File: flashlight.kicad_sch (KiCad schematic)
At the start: 25 parts, among them J1 USB_B_Micro, J2 Conn_01x03_Pin, Q1 HSS2333, Q2 HSS2333, SW1 SW_DIP_x01, U1 LP4054HB5F, U2 MT3608

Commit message: tight sot23-6
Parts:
- removed R11: 10k, Resistor_SMD:R_0603_1608Metric, symbol Device:R
- U2: footprint Package_TO_SOT_SMD:SOT-23-6 -> SparkFun-Semiconductor-Standard:SOT23-6-Tight
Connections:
- net at C3.1, L1.1, SW1.2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: now also U2.4 (EN)
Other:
- moved on the sheet: C4, D5, L1, R6, R7, U2

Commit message: v2.4: double led
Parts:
- removed D2: CHARGING, LED_SMD:LED_0603_1608Metric, symbol Device:LED
- removed D3: CHARGED, LED_SMD:LED_0805_2012Metric, symbol Device:LED
- removed R3: 1k, Resistor_SMD:R_0805_2012Metric, symbol Device:R
- removed U1: LP4054HB5F, Package_TO_SOT_SMD:SOT-23-5, symbol Battery_Management:MCP73831-2-OT
- added U3: TP4057, Package_TO_SOT_SMD:SOT-23-6, symbol MySymbols:TP4057
- added U4: R6BHC-A05_LED-19-223, MyFootprints:R6BHC-A05_LED, symbol MySymbols_GLOB:R6BHC-A05_LED
- BT1: footprint FlashlightLib:BH-18650 -> FlashlightLib:BH-18650_NoHole; now not fitted
- J2, SW1: now not fitted
- L1: now in the parts list
- R1, R2: value 1k -> 2k2; footprint Resistor_SMD:R_0805_2012Metric -> Resistor_SMD:R_0603_1608Metric; LCSC C17513 -> C4190
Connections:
- net GND: now also U3.2 (GND)
- net at C2.1, Q1.3 (D), Q2.3 (D): now also U3.3 (BAT)
- net at R2.1: now also C1.1, D1.1 (K), D4.2 (A), Q2.1 (G), R4.1, U3.4 (VCC)
- net at R2.2: now also U4.1 (Blue+), U4.3 (Red+)
- net at R1.1: now also U3.6 (PROG)
- new net: U3.5 (STDBY), U4.2 (Blue-)
- new net: U3.1 (CHRG), U4.4 (Red-)

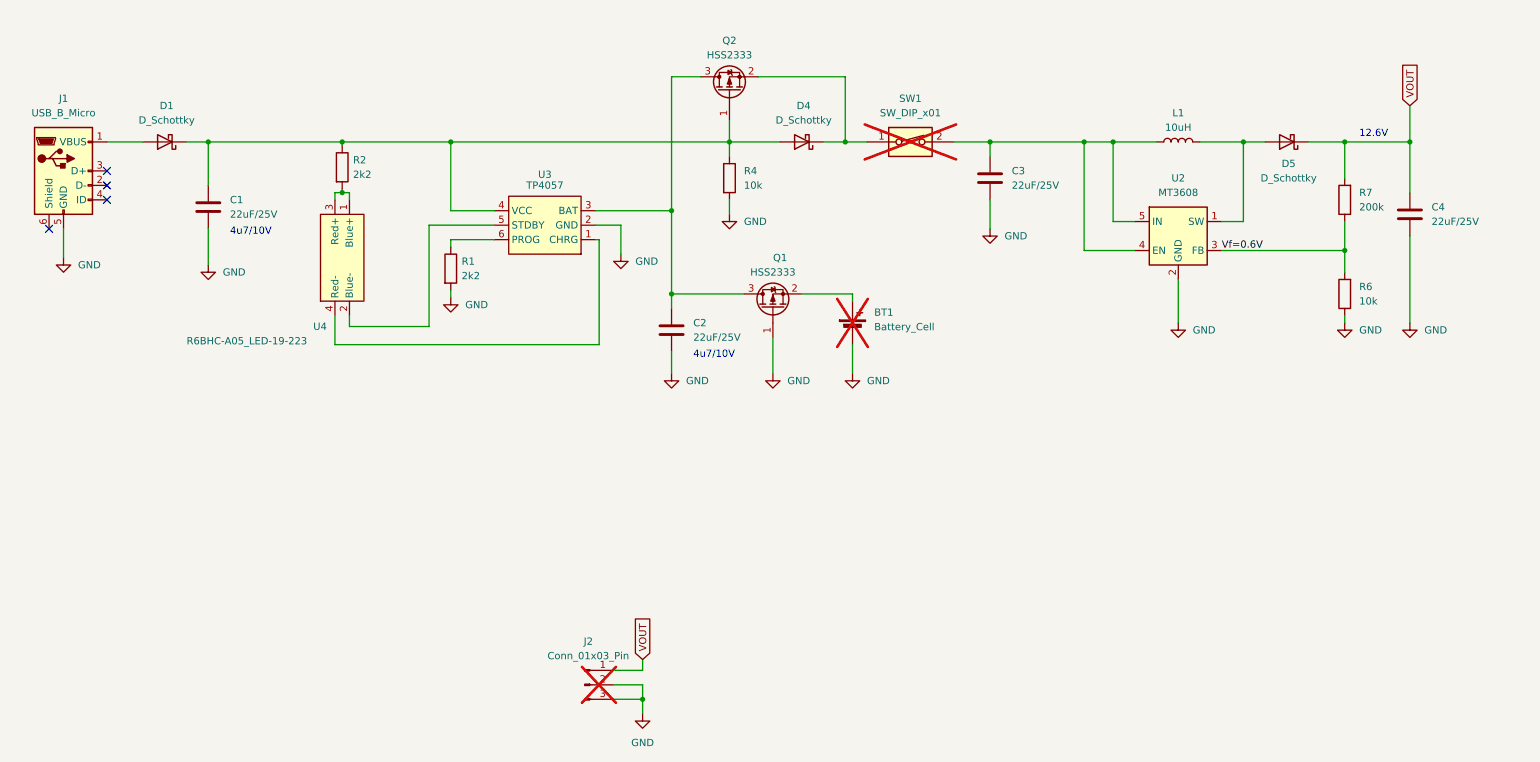
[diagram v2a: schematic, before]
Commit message: v2.4 xb4908A undervoltage protection
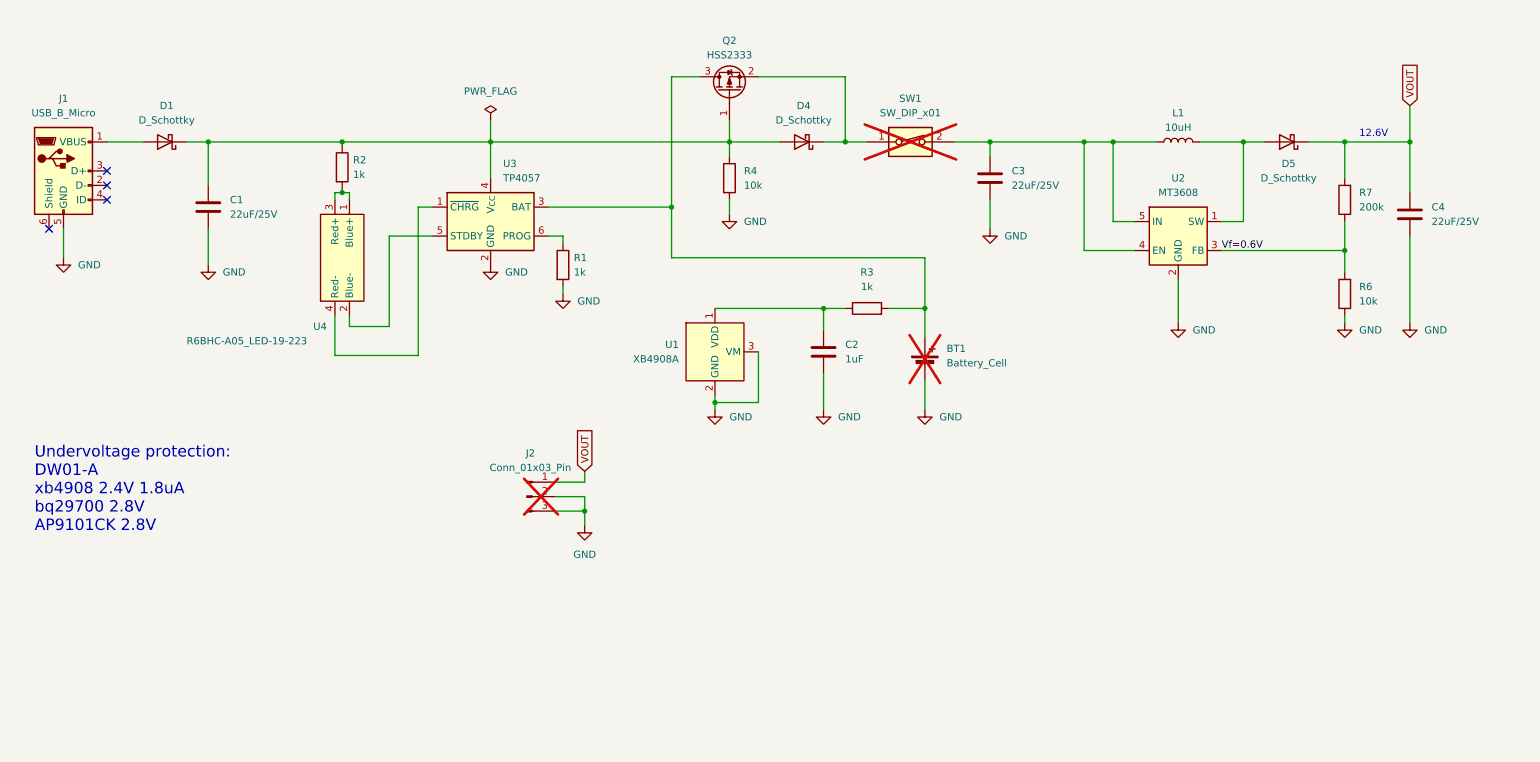
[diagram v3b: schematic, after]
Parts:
- removed Q1: HSS2333, Package_TO_SOT_SMD:SOT-23, symbol Transistor_FET:AO3401A
- removed U3: TP4057, Package_TO_SOT_SMD:SOT-23-6, symbol MySymbols:TP4057
- added R3: 1k, Resistor_SMD:R_0603_1608Metric, symbol Device:R
- added U1: XB4908A, FlashlightLib:XB4908A, symbol MySymbols:XB4908A
- added U3: TP4057, Package_TO_SOT_SMD:TSOT-23-6, symbol Battery_Management:TP4057
- C2: value 22uF/25V -> 1uF; footprint Capacitor_SMD:C_0805_2012Metric -> Capacitor_SMD:C_0603_1608Metric; LCSC C45783 -> C15849
- C3: LCSC C513764 -> C45783
- D5: LCSC C5338051 -> C22452
- R1, R2: value 2k2 -> 1k; LCSC C4190 -> C21190
- U2: footprint SparkFun-Semiconductor-Standard:SOT23-6-Tight -> Package_TO_SOT_SMD:SOT-23-6
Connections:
- net GND: now also U1.2 (GND), U1.3 (VM), U1.4 (VM), U3.2 (GND)
- net at C1.1, D1.1 (K), D4.2 (A)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: now also U3.4 (V_{CC})
- net at BT1.1 (+): now also Q2.3 (D), R3.2, U3.3 (BAT)
- net at C2.1: now also R3.1, U1.1 (VDD); no longer Q2.3 (D)
- net at U4.2 (Blue-): now also U3.5 (STDBY)
- net at U4.4 (Red-): now also U3.1 (~{CHRG})
- net at R1.1: now also U3.6 (PROG)
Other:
- note added: "Undervoltage protection: DW01-A xb4908 2.4V 1.8uA bq29700 2.8V AP9101CK 2.8V"
- note removed: "4u7/10V"
- moved on the sheet: BT1, C2, J2, R1

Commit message: increased 18650 pads size, added led stripe silkscreen line, increased switch hole length by 0.1mm
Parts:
- U3: LCSC (none) -> C12044
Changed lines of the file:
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@@
+			)
+		)
+		(property "LCSC" "C12044"
+			(at 102.87 72.39 0)
+			(effects
+				(font
+					(size 1.27 1.27)
+				)
+				(hide yes)
 			)
 		)

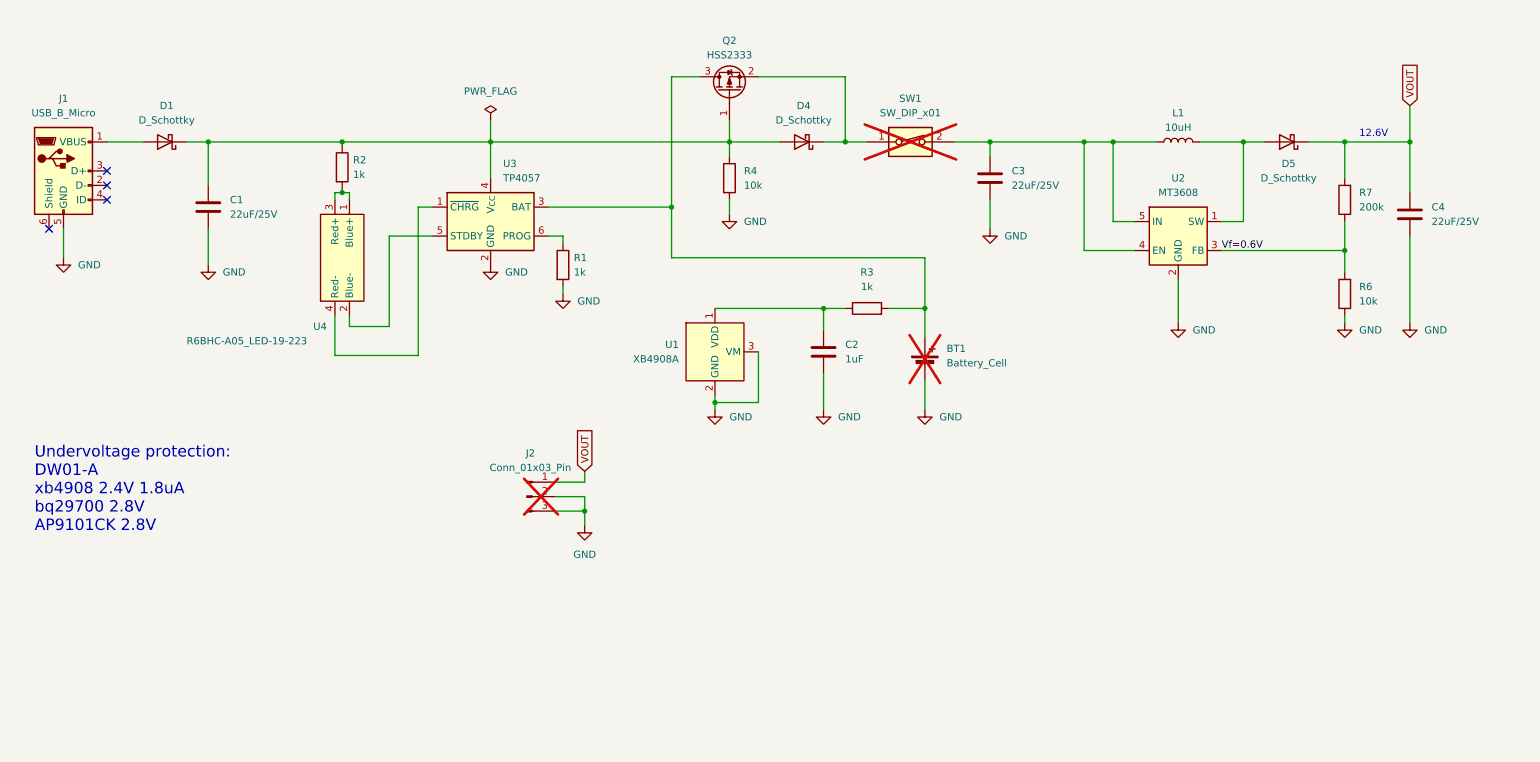
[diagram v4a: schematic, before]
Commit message: undervoltage protection only
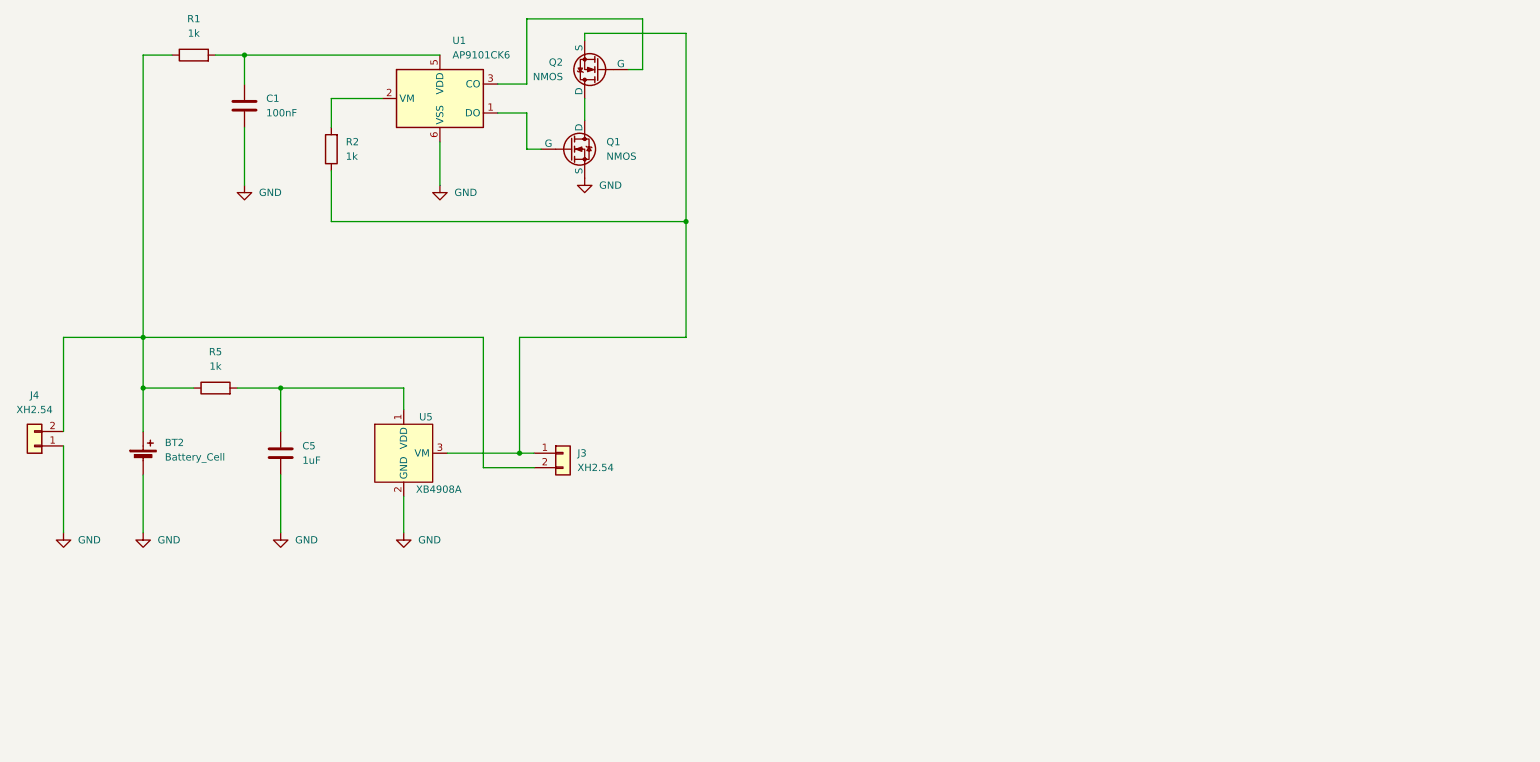
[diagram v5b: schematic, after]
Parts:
- removed BT1: Battery_Cell, FlashlightLib:BH-18650_NoHole, symbol Device:Battery_Cell
- removed C2: 1uF, Capacitor_SMD:C_0603_1608Metric, symbol Device:C
- removed C3, C4: 22uF/25V, Capacitor_SMD:C_0805_2012Metric, symbol Device:C
- removed D1, D4, D5: D_Schottky, Diode_SMD:D_SMB, symbol Device:D_Schottky
- removed J1: USB_B_Micro, FlashlightLib:USB-1101IPX6-02, symbol Connector:USB_B_Micro
- removed J2: Conn_01x03_Pin, FlashlightLib:LED_Strip, symbol Connector:Conn_01x03_Pin
- removed L1: 10uH, FlashlightLib:L_5.0x5.0, symbol Device:L
- removed Q2: HSS2333, Package_TO_SOT_SMD:SOT-23, symbol Transistor_FET:AO3401A
- removed R3: 1k, Resistor_SMD:R_0603_1608Metric, symbol Device:R
- removed R4, R6: 10k, Resistor_SMD:R_0603_1608Metric, symbol Device:R
- removed R7: 200k, Resistor_SMD:R_0603_1608Metric, symbol Device:R
- removed SW1: SW_DIP_x01, FlashlightLib:KCD11-2P, symbol Switch:SW_DIP_x01
- removed U1: XB4908A, FlashlightLib:XB4908A, symbol MySymbols:XB4908A
- removed U2: MT3608, Package_TO_SOT_SMD:SOT-23-6, symbol Regulator_Switching:MT3608
- removed U3: TP4057, Package_TO_SOT_SMD:TSOT-23-6, symbol Battery_Management:TP4057
- removed U4: R6BHC-A05_LED-19-223, MyFootprints:R6BHC-A05_LED, symbol MySymbols_GLOB:R6BHC-A05_LED
- added BT2: Battery_Cell, MyFootprints:18650_BattClip_SMD, symbol Device:Battery_Cell
- added C5: 1uF, Capacitor_SMD:C_0805_2012Metric_Pad1.18x1.45mm_HandSolder, symbol Device:C
- added J3, J4: XH2.54, MyFootprints:Conn_XH2.54-2PLT, symbol Connector_Generic:Conn_01x02
- added Q1, Q2: NMOS, MyFootprints:SOT-23-AO3400A, symbol Simulation_SPICE:NMOS
- added R5: 1k, Resistor_SMD:R_0805_2012Metric_Pad1.20x1.40mm_HandSolder, symbol Device:R
- added U1: AP9101CK6, Package_TO_SOT_SMD:SOT-23-6, symbol Battery_Management:AP9101CK6
- added U5: XB4908A, FlashlightLib:XB4908A, symbol MySymbols:XB4908A
- C1: value 22uF/25V -> 100nF; footprint Capacitor_SMD:C_0805_2012Metric -> Capacitor_SMD:C_0805_2012Metric_Pad1.18x1.45mm_HandSolder; LCSC C45783 -> C15849
- R1, R2: footprint Resistor_SMD:R_0603_1608Metric -> Resistor_SMD:R_0805_2012Metric_Pad1.20x1.40mm_HandSolder
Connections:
- net GND: now also BT2.2 (-), C5.2, J4.1 (Pin_1), Q1.3 (S), U1.6 (VSS), U5.2 (GND); no longer R1.2
- net at R2.1: now also J3.1 (Pin_1), Q2.3 (S), U5.3 (VM), U5.4 (VM); no longer C1.1
- net at R2.2: now also U1.2 (VM)
- net at R1.1: now also BT2.1 (+), J3.2 (Pin_2), J4.2 (Pin_2), R5.1
- new net: Q1.1 (D), Q2.1 (D)
- new net: Q1.2 (G), U1.1 (DO)
- new net: Q2.2 (G), U1.3 (CO)
- new net: C1.1, R1.2, U1.5 (VDD)
- new net: C5.1, R5.2, U5.1 (VDD)
- no-connect marks 4 -> 0
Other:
- note removed: "12.6V"
- note removed: "Undervoltage protection: DW01-A xb4908 2.4V 1.8uA bq29700 2.8V AP9101CK 2.8V"
